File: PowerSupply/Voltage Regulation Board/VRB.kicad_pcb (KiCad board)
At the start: 2 copper layers, 34.2 x 45.8 mm, 14 parts, among them J301 16PinConnector, J401 8PinConnector

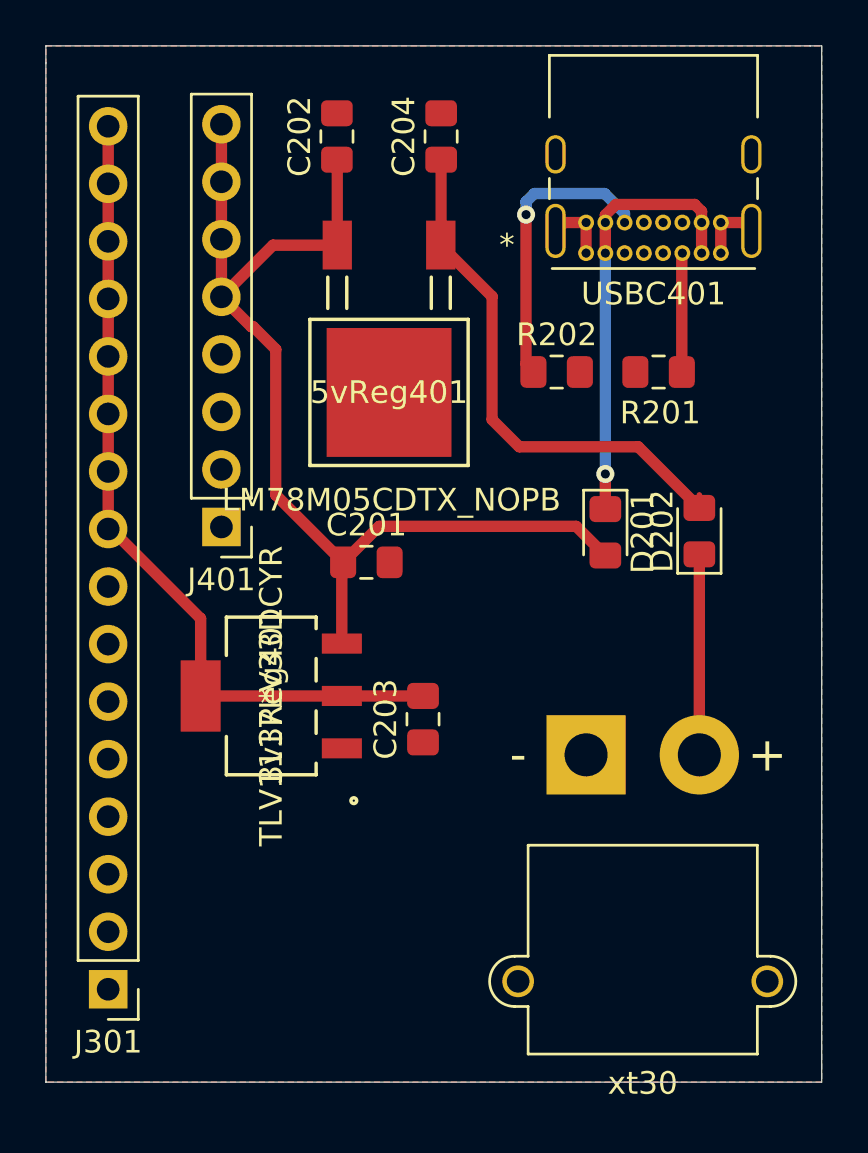
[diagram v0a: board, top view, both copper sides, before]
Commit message: Fixed the Silk Screen
Looks all pretty now
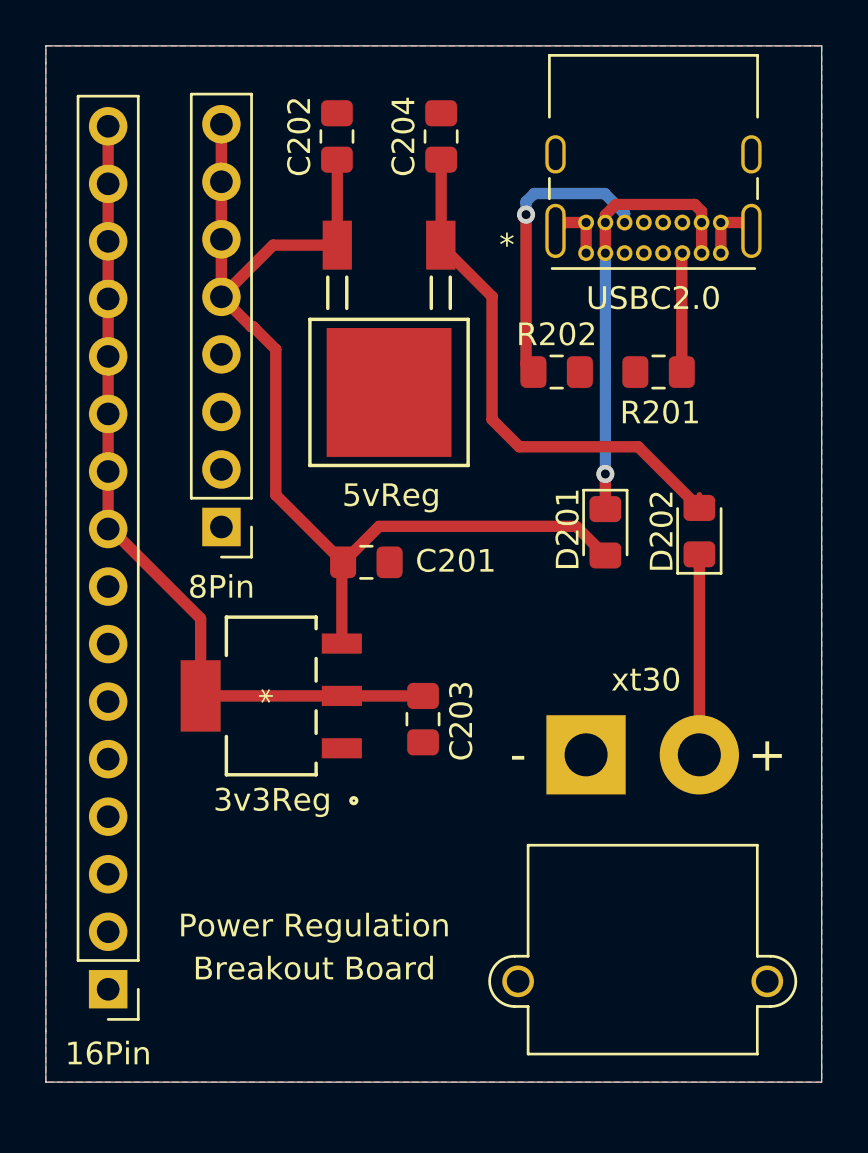
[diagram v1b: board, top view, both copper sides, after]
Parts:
- 3v3Reg: renamed from 3v3Reg401; value TLV1117LV33DCYR -> (none)
- 5vReg: renamed from 5vReg401; value LM78M05CDTX_NOPB -> (none)
- renumbered J301 to 16Pin, J401 to 8Pin, USBC401 to USBC2.0
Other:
- board text added: "Breakout Board"
- board text added: "Power Regulation"
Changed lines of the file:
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@@
   (general
     (thickness 1.6)
-    (drawings 7)
+    (drawings 9)
     (tracks 65)
     (zones 0)
@@
   (page A4)
   (layers
-    (0 F.Cu signal)
-    (31 B.Cu signal)
+    (0 F.Cu signal hide)
+    (31 B.Cu signal hide)
     (32 B.Adhes user)
     (33 F.Adhes user)
@@
   )
   (setup
-    (last_trace_width 0.5)
+    (last_trace_width 0.25)
     (user_trace_width 0.5)
     (trace_clearance 0.2)
@@
   (module FootprintLibrary:TLV1117LV33DCYR (layer F.Cu)
     (at 114.2 82.7 90)
-    (fp_text reference 3v3Reg401 (at 0 0 90) (layer F.SilkS)
-      (effects (font (size 1 1) (thickness 0.15)))
-    )
-    (fp_text value TLV1117LV33DCYR (at 0 0 90) (layer F.SilkS)
+    (fp_text reference 3v3Reg (at -4.6 0.05 180) (layer F.SilkS)
+      (effects (font (size 1 1) (thickness 0.15)))
+    )
+    (fp_text value " " (at -3 3.55 90) (layer F.SilkS)
       (effects (font (size 1 1) (thickness 0.15)))
     )
@@
   (module FootprintLibrary:LM78M05CDTX&slash_NOPB (layer F.Cu)
     (at 119.4 69.3 180)
-    (fp_text reference 5vReg401 (at 0 0) (layer F.SilkS)
-      (effects (font (size 1 1) (thickness 0.15)))
-    )
-    (fp_text value LM78M05CDTX_NOPB (at -0.1 -4.75) (layer F.SilkS)
+    (fp_text reference 5vReg (at -0.1 -4.55) (layer F.SilkS)
+      (effects (font (size 1 1) (thickness 0.15)))
+    )
+    (fp_text value " " (at -0.1 -4.75) (layer F.SilkS)
       (effects (font (size 1 1) (thickness 0.15)))
     )
@@
     (tags "capacitor handsolder")
     (attr smd)
-    (fp_text reference C201 (at 0 -1.65) (layer F.SilkS)
+    (fp_text reference C201 (at 3.95 -0.05) (layer F.SilkS)
       (effects (font (size 1 1) (thickness 0.15)))
     )
@@
     (tags "capacitor handsolder")
     (attr smd)
-    (fp_text reference C203 (at 0 -1.65 90) (layer F.SilkS)
+    (fp_text reference C203 (at -0.075 1.7 90) (layer F.SilkS)
       (effects (font (size 1 1) (thickness 0.15)))
     )
@@
     (tags "diode handsolder")
     (attr smd)
-    (fp_text reference D201 (at 0 -1.65 90) (layer F.SilkS)
+    (fp_text reference D201 (at -0.125 1.65 90) (layer F.SilkS)
       (effects (font (size 1 1) (thickness 0.15)))
     )
@@
     (descr "Through hole straight pin header, 1x16, 2.54mm pitch, single row")
     (tags "Through hole pin header THT 1x16 2.54mm single row")
-    (fp_text reference J301 (at 0 -2.33) (layer F.SilkS)
+    (fp_text reference 16Pin (at 0 -2.85) (layer F.SilkS)
       (effects (font (size 1 1) (thickness 0.15)))
     )
@@
     (descr "Through hole straight pin header, 1x08, 2.54mm pitch, single row")
     (tags "Through hole pin header THT 1x08 2.54mm single row")
-    (fp_text reference J401 (at 0 -2.33) (layer F.SilkS)
+    (fp_text reference 8Pin (at 0 -2.66) (layer F.SilkS)
       (effects (font (size 1 1) (thickness 0.15)))
     )
@@
     (descr "USB 2.0 Type C Receptacle, https://gct.co/Files/Drawings/USB4085.pdf")
     (tags "USB Type-C Receptacle Through-hole Right angle")
-    (fp_text reference USBC401 (at 2.975 -1.8) (layer F.SilkS)
+    (fp_text reference USBC2.0 (at 2.975 -2) (layer F.SilkS)
       (effects (font (size 1 1) (thickness 0.15)))
     )
@@
     (descr "Connector XT30 Horizontal PCB Male, https://www.tme.eu/en/Document/ce4077e36b79046da520ca73227e15de/XT30PW%20SPEC.pdf")
     (tags "RC Connector XT30")
-    (fp_text reference xt30 (at -2.5 -14.5) (layer F.SilkS)
+    (fp_text reference xt30 (at -2.65 3.3) (layer F.SilkS)
       (effects (font (size 1 1) (thickness 0.15)))
     )
@@
     )
   )
+  (gr_text "Breakout Board" (at 116.1 94.75) (layer F.SilkS)
+    (effects (font (size 1 1) (thickness 0.15)))
+  )
+  (gr_text "Power Regulation" (at 116.1 92.85) (layer F.SilkS)
+    (effects (font (size 1 1) (thickness 0.15)))
+  )
   (gr_line (start 104.25 54) (end 104.25 54.75) (layer Edge.Cuts) (width 0.05))
   (gr_line (start 138 54) (end 104.25 54) (layer Edge.Cuts) (width 0.05))
@@
   (gr_line (start 138.5 54) (end 138 54) (layer Edge.Cuts) (width 0.05))
   (gr_line (start 138.5 99.75) (end 138.5 54) (layer Edge.Cuts) (width 0.05))
+  (segment (start 117.55 66.832599) (end 117.565001 66.8476) (width 0.25) (layer F.Cu) (net 1))
+  (segment (start 134.05 61.8) (end 134.05 63.15) (width 0.5) (layer F.Cu) (net 1))
+  (segment (start 135.03 61.8) (end 135.4 62.17) (width 0.5) (layer F.Cu) (net 1))
+  (segment (start 134.05 61.8) (end 135.03 61.8) (width 0.5) (layer F.Cu) (net 1))
+  (segment (start 128.1 61.8) (end 128.1 63.15) (width 0.5) (layer F.Cu) (net 1))
+  (segment (start 127.12 61.8) (end 126.75 62.17) (width 0.5) (layer F.Cu) (net 1))
+  (segment (start 128.1 61.8) (end 127.12 61.8) (width 0.5) (layer F.Cu) (net 1))
   (segment (start 120.9 82.7) (end 117.31785 82.7) (width 0.5) (layer F.Cu) (net 2))
   (segment (start 117.31785 82.7) (end 111.08215 82.7) (width 0.5) (layer F.Cu) (net 2))
@@
   (segment (start 107 75.33) (end 107 57.55) (width 0.5) (layer F.Cu) (net 2))
   (segment (start 112.0376 57.4976) (end 112 57.46) (width 0.25) (layer F.Cu) (net 3))
-  (segment (start 117.55 66.832599) (end 117.565001 66.8476) (width 0.25) (layer F.Cu) (net 1))
-  (segment (start 134.05 61.8) (end 134.05 63.15) (width 0.5) (layer F.Cu) (net 1))
-  (segment (start 135.03 61.8) (end 135.4 62.17) (width 0.5) (layer F.Cu) (net 1))
-  (segment (start 134.05 61.8) (end 135.03 61.8) (width 0.5) (layer F.Cu) (net 1))
-  (segment (start 128.1 61.8) (end 128.1 63.15) (width 0.5) (layer F.Cu) (net 1))
-  (segment (start 127.12 61.8) (end 126.75 62.17) (width 0.5) (layer F.Cu) (net 1))
-  (segment (start 128.1 61.8) (end 127.12 61.8) (width 0.5) (layer F.Cu) (net 1))
   (segment (start 117.32925 80.4) (end 117.31785 80.3886) (width 0.25) (layer F.Cu) (net 3))
   (segment (start 117.375 80.33145) (end 117.31785 80.3886) (width 0.25) (layer F.Cu) (net 3))

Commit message: Fixed Diode Thingy
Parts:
- removed D202: DIODE, Diode_SMD:D_0805_2012Metric_Pad1.15x1.40mm_HandSolder
- 3v3Reg401: renamed from 3v3Reg; value (none) -> TLV1117LV33DCYR
- 5vReg401: renamed from 5vReg; value (none) -> LM78M05CDTX_NOPB
- renumbered 16Pin to J301, 8Pin to J401, USBC2.0 to USBC401
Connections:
- xt30 pad 2: Net-(D202-Pad1) -> Net-(5vReg401-Pad1)
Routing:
- net Net-(5vReg401-Pad1): track 23.8 -> 34.1 mm
- net Net-(D202-Pad1): track 8.85 -> 0.00 mm
